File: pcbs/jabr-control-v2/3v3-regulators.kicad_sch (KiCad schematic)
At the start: 35 parts, among them U1401 TPS62290TDRVRQ1, U401 LMQ66430MC3RXBRQ1, U402 TPS7B8133QDRVRQ1, U403 TPS2116DRL

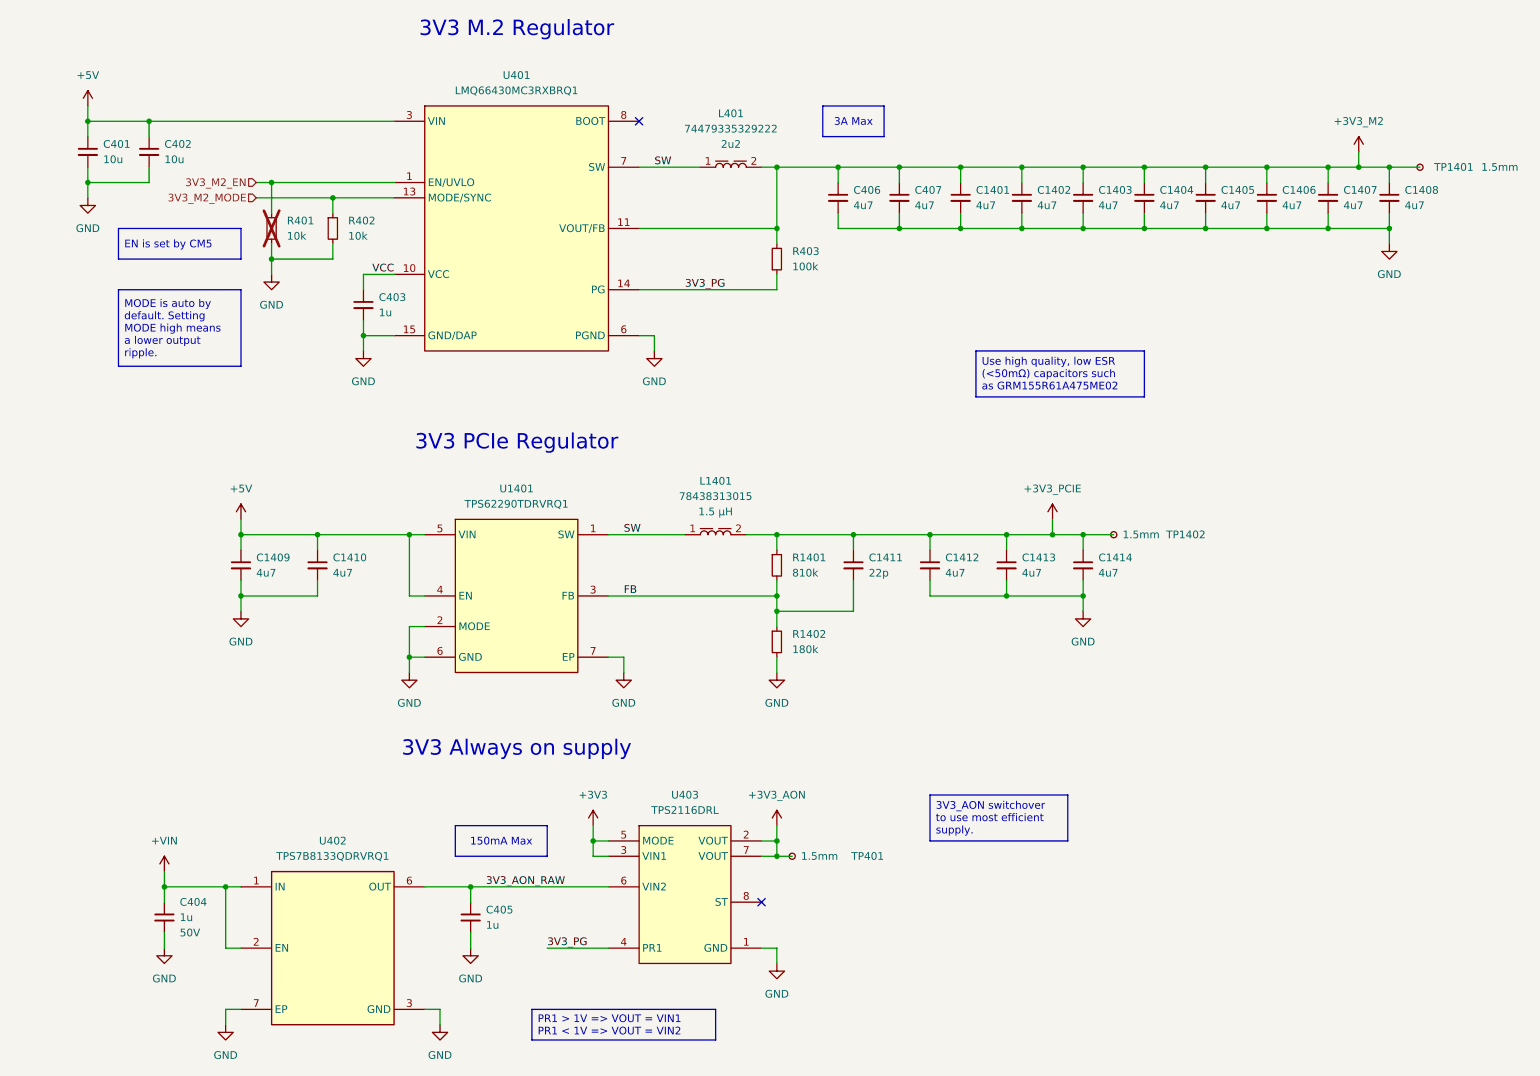
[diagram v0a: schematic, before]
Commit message: PCI11010C Schematic sheet mostly done
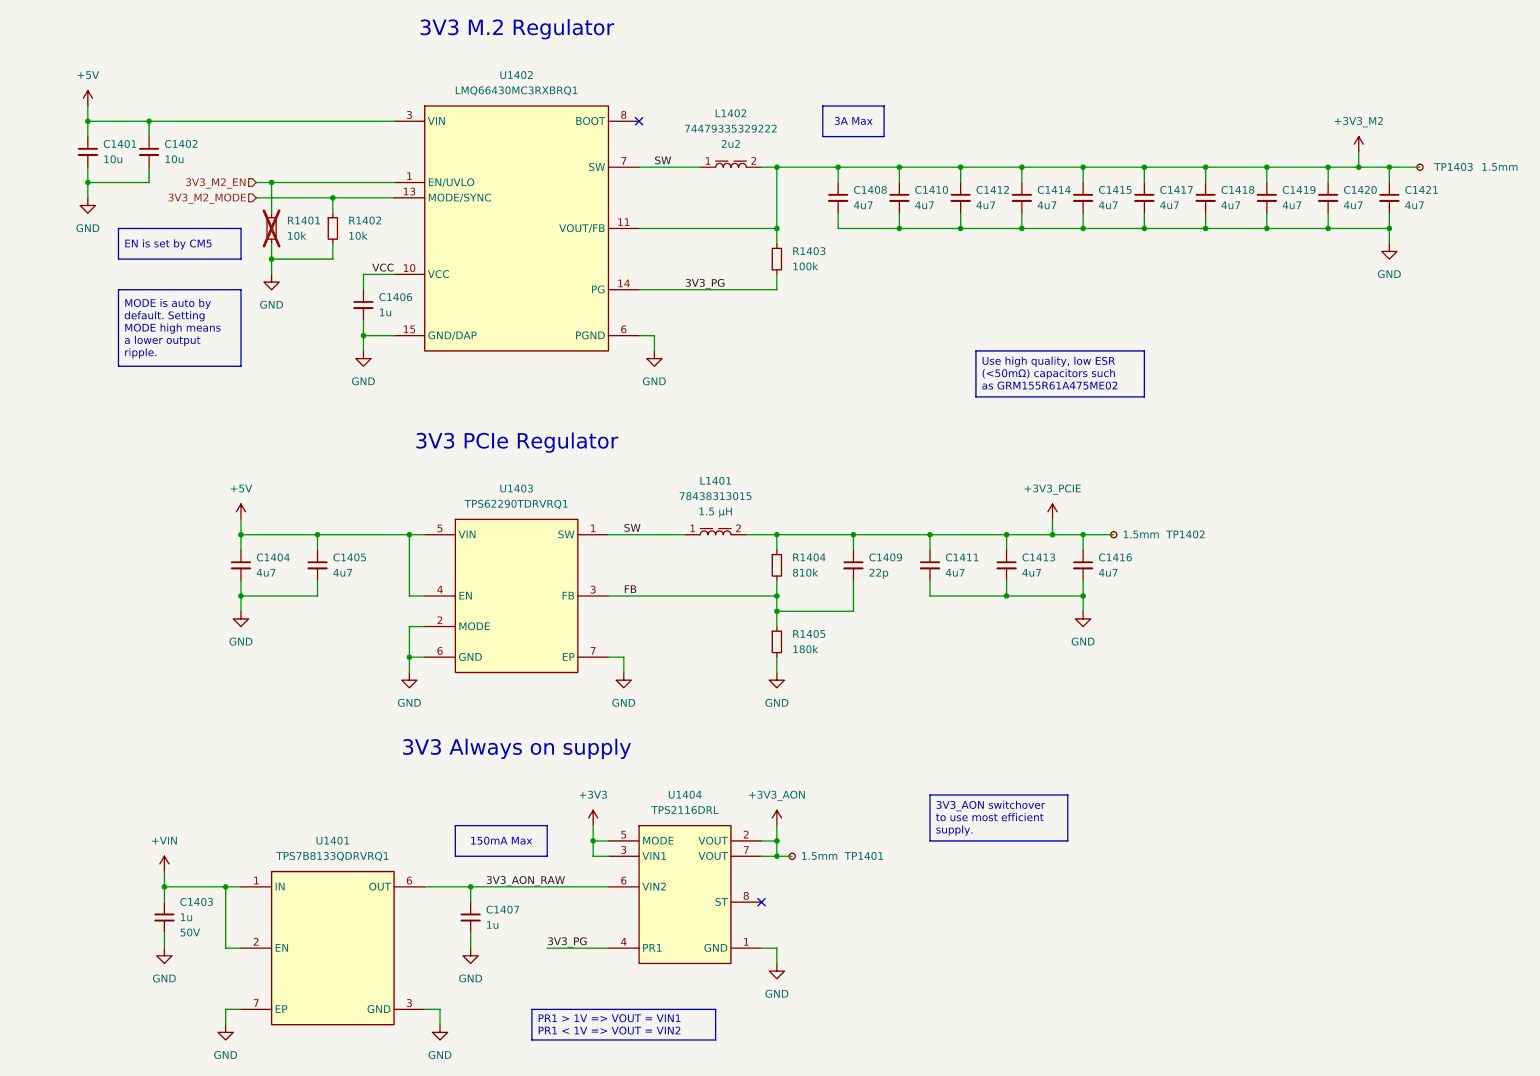
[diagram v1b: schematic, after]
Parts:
- renumbered C401 to C1401, C402 to C1402, C404 to C1403, C1409 to C1404, C1410 to C1405, C403 to C1406, C405 to C1407, C406 to C1408, C1411 to C1409, C407 to C1410, C1412 to C1411, C1401 to C1412, C1402 to C1414, C1403 to C1415, C1414 to C1416, C1404 to C1417, C1405 to C1418, C1406 to C1419, C1407 to C1420, C1408 to C1421, L401 to L1402, R401 to R1401, R402 to R1402, R403 to R1403, R1401 to R1404, R1402 to R1405, TP401 to TP1401, TP1401 to TP1403, U402 to U1401, U401 to U1402, U1401 to U1403, U403 to U1404

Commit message: Moved M.2 buffers to new sheet
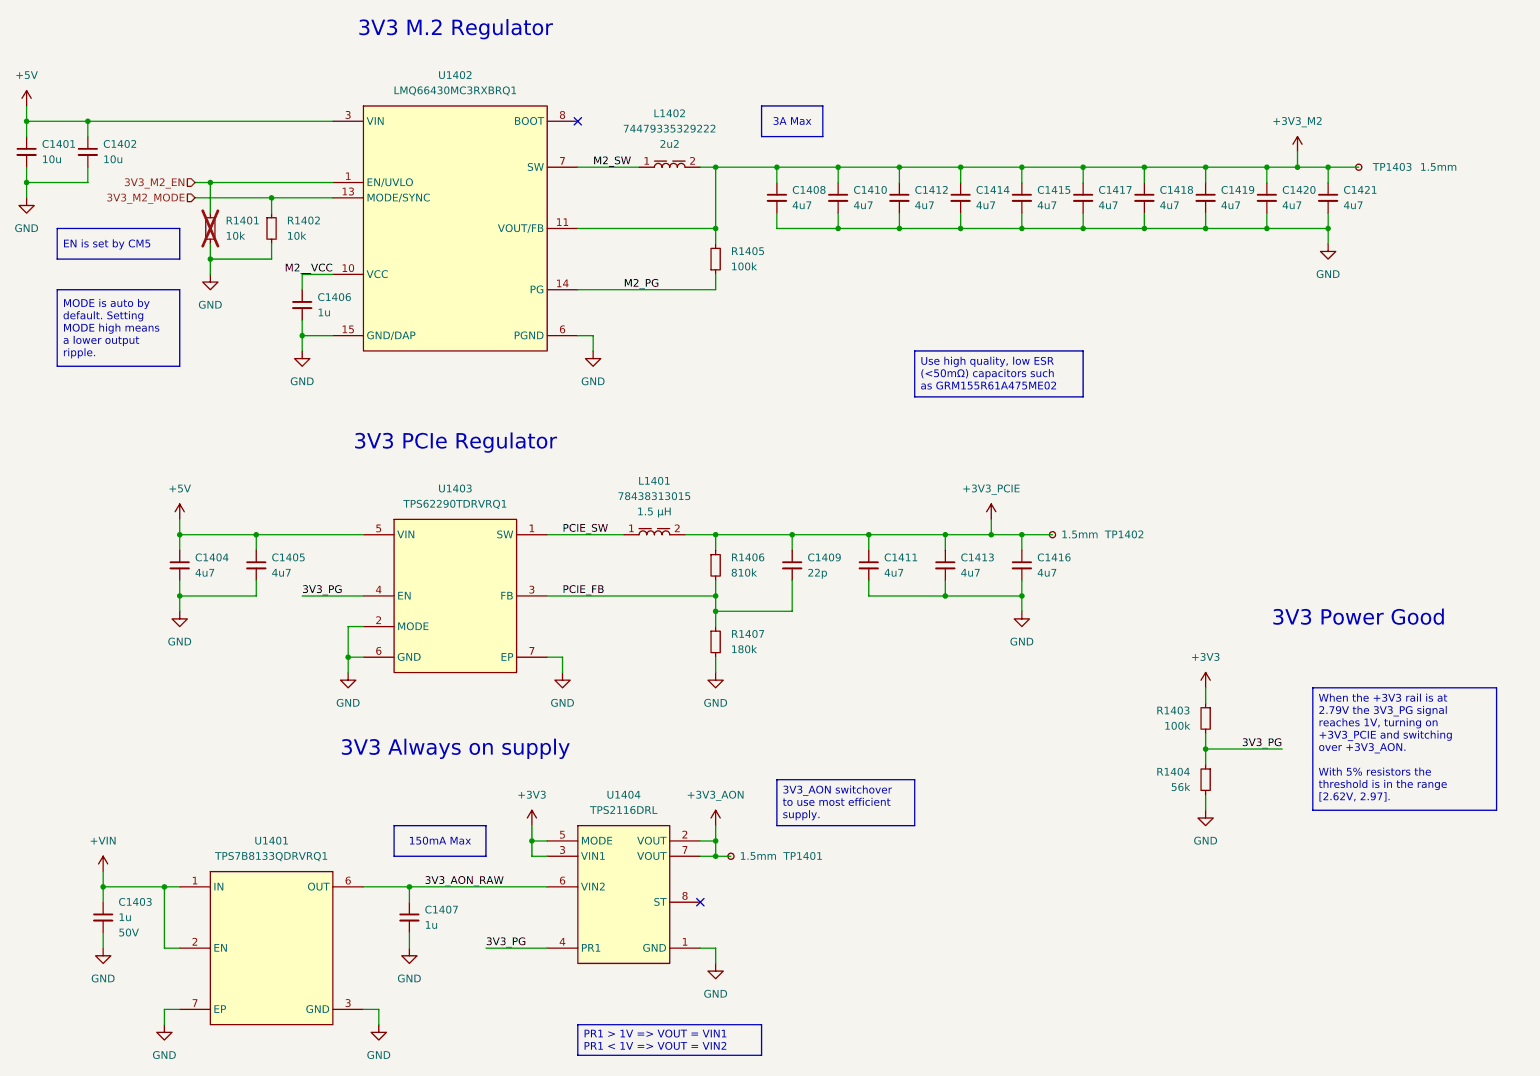
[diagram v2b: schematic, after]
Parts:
- added R1403: 100k, project_footprints:R_0402, symbol Device:R_Small
- added R1404: 56k, project_footprints:R_0402, symbol Device:R_Small
- renumbered R1403 to R1405, R1404 to R1406, R1405 to R1407
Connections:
- net +3V3: now also R1403.1
- net +5V: no longer U1403.4 (EN)
- net 3V3_PG: now also U1403.4 (EN), R1403.2, R1404.1; no longer R1405.1, U1402.14 (PG)
- net GND: now also R1404.2
- net FB renamed PCIE_FB
- net SW renamed M2_SW
- net M2_SW: no longer L1401.1, U1403.1 (SW)
- net VCC renamed M2__VCC
- new net M2_PG: R1405.1, U1402.14 (PG)
- new net PCIE_SW: L1401.1, U1403.1 (SW)
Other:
- note added: "3V3 Power Good"
- moved on the sheet: C1401, C1402, C1403, C1404, C1405, C1406, C1407, C1408, C1409, C1410, C1411, C1412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
